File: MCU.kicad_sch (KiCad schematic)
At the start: 16 parts, among them U4 EFM32GG332, Y1 Crystal_GND23

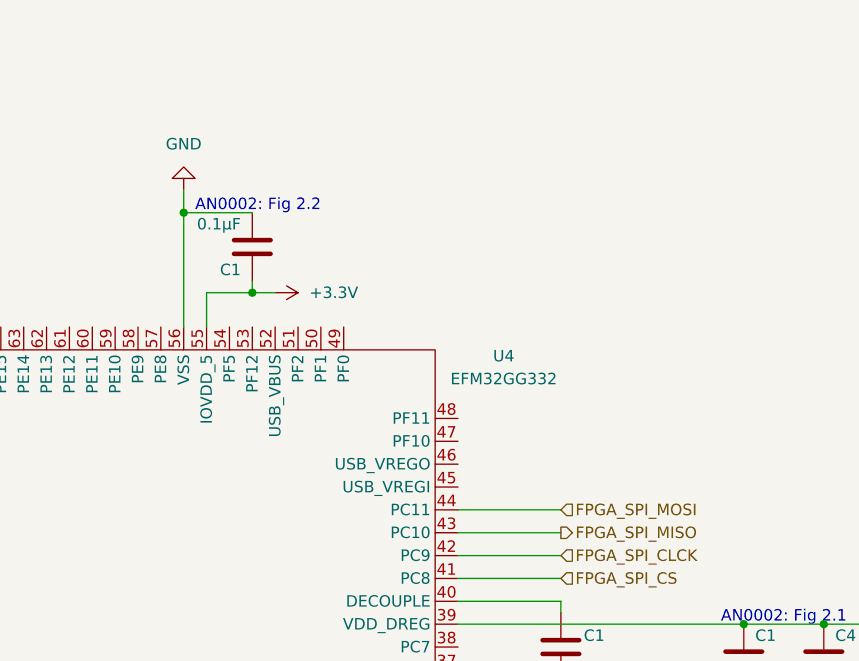
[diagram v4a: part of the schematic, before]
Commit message: Added labels in root for USB signals
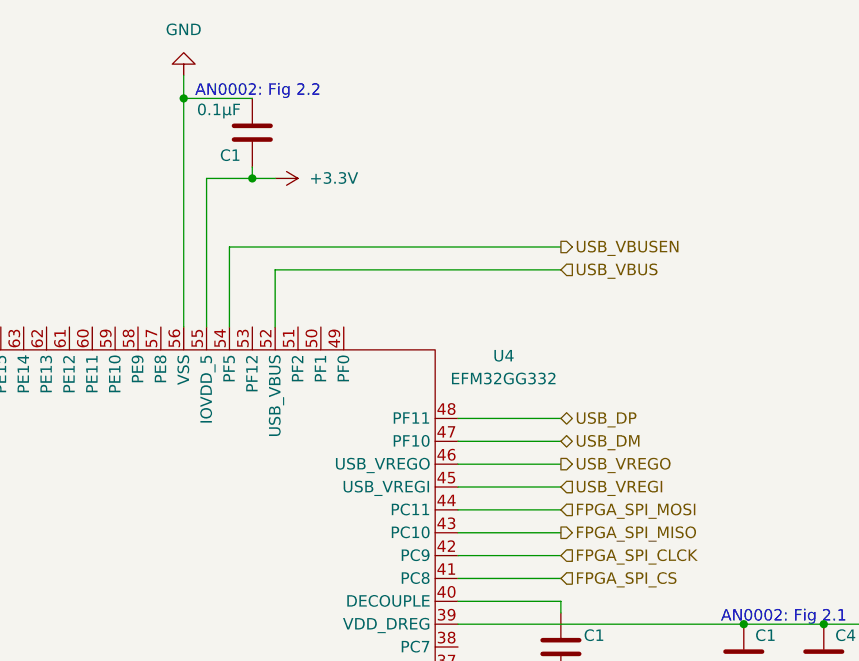
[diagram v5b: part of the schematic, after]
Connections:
- net USB_VREGI: now reaches U4.45 (USB_VREGI)
- net USB_VREGO: now reaches U4.46 (USB_VREGO)
- net USB_DM: now reaches U4.47 (PF10)
- net USB_DP: now reaches U4.48 (PF11)
- net USB_VBUS: now reaches U4.52 (USB_VBUS)
- net USB_VBUSEN: now reaches U4.54 (PF5)
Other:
- moved on the sheet: C1
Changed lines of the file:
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@@
   (junction (at 104.14 133.35) (diameter 0) (color 0 0 0 0)
   )
-  (junction (at 139.7 45.72) (diameter 0) (color 0 0 0 0)
+  (junction (at 139.7 33.02) (diameter 0) (color 0 0 0 0)
   )
   (junction (at 185.42 147.32) (diameter 0) (color 0 0 0 0)
@@
   (junction (at 170.18 147.32) (diameter 0) (color 0 0 0 0)
   )
-  (junction (at 147.32 54.61) (diameter 0) (color 0 0 0 0)
+  (junction (at 147.32 41.91) (diameter 0) (color 0 0 0 0)
   )
   (junction (at 134.62 133.35) (diameter 0) (color 0 0 0 0)
@@
   (junction (at 123.19 133.35) (diameter 0) (color 0 0 0 0)
   )
+  (wire (pts (xy 170.18 73.66) (xy 181.61 73.66))
+    (stroke (width 0) (type default))
+  )
   (wire (pts (xy 185.42 147.32) (xy 182.88 147.32))
     (stroke (width 0) (type default))
@@
     (stroke (width 0) (type default))
   )
+  (wire (pts (xy 144.78 58.42) (xy 144.78 49.53))
+    (stroke (width 0) (type default))
+  )
   (wire (pts (xy 101.6 81.28) (xy 106.68 81.28))
     (stroke (width 0) (type default))
@@
     (stroke (width 0) (type default))
   )
+  (wire (pts (xy 149.86 58.42) (xy 149.86 52.07))
+    (stroke (width 0) (type default))
+  )
   (wire (pts (xy 185.42 157.48) (xy 185.42 156.21))
     (stroke (width 0) (type default))
@@
     (stroke (width 0) (type default))
   )
-  (wire (pts (xy 139.7 45.72) (xy 147.32 45.72))
+  (wire (pts (xy 139.7 33.02) (xy 147.32 33.02))
+    (stroke (width 0) (type default))
+  )
+  (wire (pts (xy 149.86 52.07) (xy 181.61 52.07))
     (stroke (width 0) (type default))
   )
@@
     (stroke (width 0) (type default))
   )
+  (wire (pts (xy 170.18 71.12) (xy 181.61 71.12))
+    (stroke (width 0) (type default))
+  )
   (wire (pts (xy 93.98 133.35) (xy 104.14 133.35))
     (stroke (width 0) (type default))
@@
     (stroke (width 0) (type default))
   )
+  (wire (pts (xy 170.18 68.58) (xy 181.61 68.58))
+    (stroke (width 0) (type default))
+  )
   (wire (pts (xy 125.73 140.97) (xy 132.08 140.97))
     (stroke (width 0) (type default))
@@
     (stroke (width 0) (type default))
   )
-  (wire (pts (xy 147.32 54.61) (xy 147.32 53.34))
+  (wire (pts (xy 147.32 41.91) (xy 147.32 40.64))
+    (stroke (width 0) (type default))
+  )
+  (wire (pts (xy 170.18 76.2) (xy 181.61 76.2))
+    (stroke (width 0) (type default))
+  )
+  (wire (pts (xy 144.78 49.53) (xy 181.61 49.53))
     (stroke (width 0) (type default))
   )
@@
     (stroke (width 0) (type default))
   )
+  (wire (pts (xy 142.24 41.91) (xy 142.24 58.42))
+    (stroke (width 0) (type default))
+  )
   (wire (pts (xy 170.18 139.7) (xy 137.16 139.7))
     (stroke (width 0) (type default))
   )
-  (wire (pts (xy 147.32 54.61) (xy 149.86 54.61))
+  (wire (pts (xy 147.32 41.91) (xy 149.86 41.91))
     (stroke (width 0) (type default))
   )
@@
     (stroke (width 0) (type default))
   )
-  (wire (pts (xy 139.7 43.18) (xy 139.7 45.72))
+  (wire (pts (xy 139.7 30.48) (xy 139.7 33.02))
     (stroke (width 0) (type default))
   )
@@
     (stroke (width 0) (type default))
   )
-  (wire (pts (xy 139.7 45.72) (xy 139.7 58.42))
+  (wire (pts (xy 139.7 33.02) (xy 139.7 58.42))
     (stroke (width 0) (type default))
   )
@@
     (stroke (width 0) (type default))
   )
-  (wire (pts (xy 142.24 58.42) (xy 142.24 54.61))
-    (stroke (width 0) (type default))
-  )
   (wire (pts (xy 125.73 133.35) (xy 134.62 133.35))
     (stroke (width 0) (type default))
@@
     (stroke (width 0) (type default))
   )
-  (wire (pts (xy 142.24 54.61) (xy 147.32 54.61))
+  (wire (pts (xy 142.24 41.91) (xy 147.32 41.91))
     (stroke (width 0) (type default))
   )
@@
     (effects (font (size 1.27 1.27)) (justify left bottom))
   )
-  (text "AN0002: Fig 2.2" (at 140.97 45.72 0)
+  (text "AN0002: Fig 2.2" (at 140.97 33.02 0)
     (effects (font (size 1.27 1.27)) (justify left bottom))
   )
@@
     (effects (font (size 1.27 1.27)) (justify right bottom))
   )
+  (hierarchical_label "USB_DM" (shape bidirectional) (at 181.61 71.12 0) (fields_autoplaced)
+    (effects (font (size 1.27 1.27)) (justify left))
+  )
   (hierarchical_label "FPGA_SPI_CS" (shape input) (at 181.61 86.36 0) (fields_autoplaced)
     (effects (font (size 1.27 1.27)) (justify left))
   )
+  (hierarchical_label "USB_VBUSEN" (shape output) (at 181.61 49.53 0) (fields_autoplaced)
+    (effects (font (size 1.27 1.27)) (justify left))
+  )
   (hierarchical_label "FPGA_SPI_CLCK" (shape input) (at 181.61 83.82 0) (fields_autoplaced)
+    (effects (font (size 1.27 1.27)) (justify left))
+  )
+  (hierarchical_label "USB_VREGI" (shape input) (at 181.61 76.2 0) (fields_autoplaced)
     (effects (font (size 1.27 1.27)) (justify left))
   )
@@
     (effects (font (size 1.27 1.27)) (justify right))
   )
+  (hierarchical_label "USB_VBUS" (shape input) (at 181.61 52.07 0) (fields_autoplaced)
+    (effects (font (size 1.27 1.27)) (justify left))
+  )
   (hierarchical_label "FPGA_RESET" (shape output) (at 161.29 121.92 0) (fields_autoplaced)
     (effects (font (size 1.27 1.27)) (justify left))
@@
     (effects (font (size 1.27 1.27)) (justify right))
   )
+  (hierarchical_label "USB_VREGO" (shape output) (at 181.61 73.66 0) (fields_autoplaced)
+    (effects (font (size 1.27 1.27)) (justify left))
+  )
   (hierarchical_label "FPGA_SPI_MOSI" (shape input) (at 181.61 78.74 0) (fields_autoplaced)
     (effects (font (size 1.27 1.27)) (justify left))
@@
   (hierarchical_label "Button 6" (shape input) (at 101.6 81.28 180) (fields_autoplaced)
     (effects (font (size 1.27 1.27)) (justify right))
+  )
+  (hierarchical_label "USB_DP" (shape bidirectional) (at 181.61 68.58 0) (fields_autoplaced)
+    (effects (font (size 1.27 1.27)) (justify left))
   )
   (hierarchical_label "Button 4" (shape input) (at 101.6 76.2 180) (fields_autoplaced)
@@
     )
   )
-  (symbol (lib_id "power:+3.3V") (at 149.86 54.61 270) (unit 1)
+  (symbol (lib_id "power:+3.3V") (at 149.86 41.91 270) (unit 1)
     (in_bom yes) (on_board yes) (dnp no) (fields_autoplaced)
-    (property "Reference" "#PWR040" (at 146.05 54.61 0)
-      (effects (font (size 1.27 1.27)) hide)
-    )
-    (property "Value" "+3.3V" (at 153.67 54.61 90)
-      (effects (font (size 1.27 1.27)) (justify left))
-    )
-    (property "Footprint" "" (at 149.86 54.61 0)
-      (effects (font (size 1.27 1.27)) hide)
-    )
-    (property "Datasheet" "" (at 149.86 54.61 0)
+    (property "Reference" "#PWR040" (at 146.05 41.91 0)
+      (effects (font (size 1.27 1.27)) hide)
+    )
+    (property "Value" "+3.3V" (at 153.67 41.91 90)
+      (effects (font (size 1.27 1.27)) (justify left))
+    )
+    (property "Footprint" "" (at 149.86 41.91 0)
+      (effects (font (size 1.27 1.27)) hide)
+    )
+    (property "Datasheet" "" (at 149.86 41.91 0)
       (effects (font (size 1.27 1.27)) hide)
     )
@@
     )
   )
-  (symbol (lib_id "Device:C") (at 147.32 49.53 180) (unit 1)
+  (symbol (lib_id "Device:C") (at 147.32 36.83 180) (unit 1)
     (in_bom yes) (on_board yes) (dnp no)
-    (property "Reference" "C1" (at 146.05 52.07 0)
-      (effects (font (size 1.27 1.27)) (justify left))
-    )
-    (property "Value" "0.1µF" (at 146.05 46.99 0)
-      (effects (font (size 1.27 1.27)) (justify left))
-    )
-    (property "Footprint" "" (at 146.3548 45.72 0)
-      (effects (font (size 1.27 1.27)) hide)
-    )
-    (property "Datasheet" "~" (at 147.32 49.53 0)
+    (property "Reference" "C1" (at 146.05 39.37 0)
+      (effects (font (size 1.27 1.27)) (justify left))
+    )
+    (property "Value" "0.1µF" (at 146.05 34.29 0)
+      (effects (font (size 1.27 1.27)) (justify left))
+    )
+    (property "Footprint" "" (at 146.3548 33.02 0)
+      (effects (font (size 1.27 1.27)) hide)
+    )
+    (property "Datasheet" "~" (at 147.32 36.83 0)
       (effects (font (size 1.27 1.27)) hide)
     )
@@
     )
   )
-  (symbol (lib_id "power:GND") (at 139.7 43.18 180) (unit 1)
+  (symbol (lib_id "power:GND") (at 139.7 30.48 180) (unit 1)
     (in_bom yes) (on_board yes) (dnp no) (fields_autoplaced)
-    (property "Reference" "#PWR01" (at 139.7 36.83 0)
-      (effects (font (size 1.27 1.27)) hide)
-    )
-    (property "Value" "GND" (at 139.7 38.1 0)
-      (effects (font (size 1.27 1.27)))
-    )
-    (property "Footprint" "" (at 139.7 43.18 0)
-      (effects (font (size 1.27 1.27)) hide)
-    )
-    (property "Datasheet" "" (at 139.7 43.18 0)
-      (effects (font (size 1.27 1.27)) hide)
-    )
+    (property "Reference" "#PWR01" (at 139.7 24.13 0)
+      (effects (font (size 1.27 1.27)) hide)
+    )
+    (property "Value" "GND" (at 139.7 25.4 0)
+      (effects (font (size 1.27 1.27)))
+    )
+    (property "Footprint" "" (at 139.7 30.48 0)
+      (effects (font (size 1.27 1.27)) hide)
+    )
+    (property "Datasheet" "" (at 139.7 30.48 0)
+      (effects (font (size 1.27 1.27)) hide)
+    )

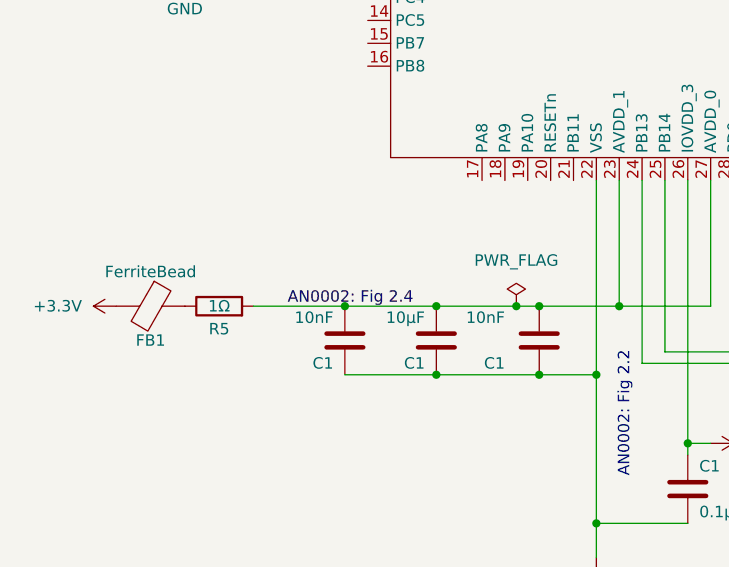
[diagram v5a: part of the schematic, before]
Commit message: Changed AVCC from ferrite bead to 3.3VA
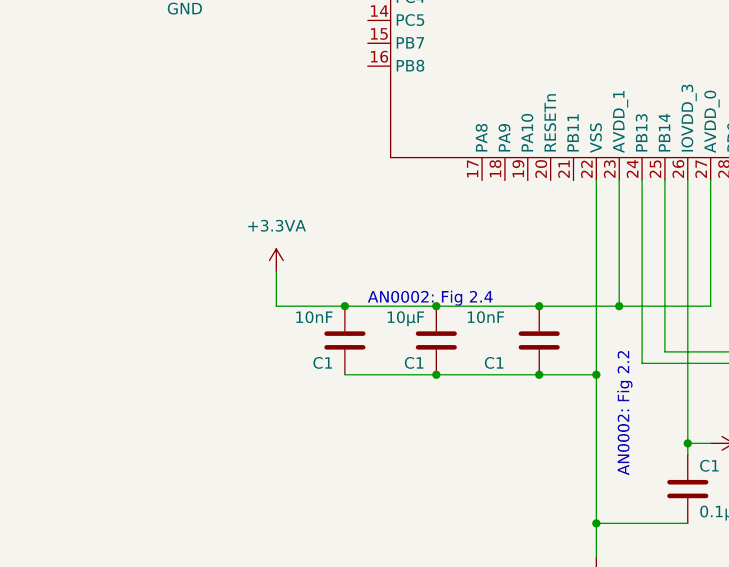
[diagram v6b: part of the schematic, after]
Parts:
- removed FB1: FerriteBead, symbol Device:FerriteBead
- removed R5: 1Ω, symbol Device:R
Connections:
- net AN0002: Fig 2.4 renamed +3.3VA
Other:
- note added: "AN0002: Fig 2.4"
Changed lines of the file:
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@@
   (junction (at 142.24 148.59) (diameter 0) (color 0 0 0 0)
   )
+  (junction (at 139.7 33.02) (diameter 0) (color 0 0 0 0)
+  )
+  (junction (at 185.42 147.32) (diameter 0) (color 0 0 0 0)
+  )
+  (junction (at 132.08 140.97) (diameter 0) (color 0 0 0 0)
+  )
+  (junction (at 125.73 140.97) (diameter 0) (color 0 0 0 0)
+  )
+  (junction (at 114.3 133.35) (diameter 0) (color 0 0 0 0)
+  )
+  (junction (at 170.18 147.32) (diameter 0) (color 0 0 0 0)
+  )
+  (junction (at 147.32 41.91) (diameter 0) (color 0 0 0 0)
+  )
+  (junction (at 134.62 133.35) (diameter 0) (color 0 0 0 0)
+  )
+  (junction (at 210.82 91.44) (diameter 0) (color 0 0 0 0)
+  )
+  (junction (at 114.3 140.97) (diameter 0) (color 0 0 0 0)
+  )
   (junction (at 104.14 133.35) (diameter 0) (color 0 0 0 0)
   )
-  (junction (at 139.7 33.02) (diameter 0) (color 0 0 0 0)
-  )
-  (junction (at 185.42 147.32) (diameter 0) (color 0 0 0 0)
-  )
-  (junction (at 132.08 140.97) (diameter 0) (color 0 0 0 0)
-  )
-  (junction (at 125.73 140.97) (diameter 0) (color 0 0 0 0)
-  )
-  (junction (at 114.3 133.35) (diameter 0) (color 0 0 0 0)
-  )
-  (junction (at 170.18 147.32) (diameter 0) (color 0 0 0 0)
-  )
-  (junction (at 147.32 41.91) (diameter 0) (color 0 0 0 0)
-  )
-  (junction (at 134.62 133.35) (diameter 0) (color 0 0 0 0)
-  )
-  (junction (at 210.82 91.44) (diameter 0) (color 0 0 0 0)
-  )
-  (junction (at 114.3 140.97) (diameter 0) (color 0 0 0 0)
-  )
   (junction (at 179.07 157.48) (diameter 0) (color 0 0 0 0)
   )
-  (junction (at 123.19 133.35) (diameter 0) (color 0 0 0 0)
-  )
   (wire (pts (xy 170.18 73.66) (xy 181.61 73.66))
     (stroke (width 0) (type default))
@@
     (stroke (width 0) (type default))
   )
+  (wire (pts (xy 96.52 133.35) (xy 104.14 133.35))
+    (stroke (width 0) (type default))
+  )
   (wire (pts (xy 175.26 147.32) (xy 170.18 147.32))
     (stroke (width 0) (type default))
@@
     (stroke (width 0) (type default))
   )
-  (wire (pts (xy 93.98 133.35) (xy 104.14 133.35))
+  (wire (pts (xy 114.3 133.35) (xy 125.73 133.35))
     (stroke (width 0) (type default))
   )
@@
     (stroke (width 0) (type default))
   )
-  (wire (pts (xy 123.19 133.35) (xy 125.73 133.35))
-    (stroke (width 0) (type default))
-  )
   (wire (pts (xy 170.18 157.48) (xy 179.07 157.48))
     (stroke (width 0) (type default))
@@
     (stroke (width 0) (type default))
   )
-  (wire (pts (xy 114.3 133.35) (xy 123.19 133.35))
-    (stroke (width 0) (type default))
-  )
   (wire (pts (xy 142.24 148.59) (xy 142.24 149.86))
     (stroke (width 0) (type default))
   )
   (wire (pts (xy 179.07 157.48) (xy 179.07 158.75))
+    (stroke (width 0) (type default))
+  )
+  (wire (pts (xy 96.52 129.54) (xy 96.52 133.35))
     (stroke (width 0) (type default))
   )
@@
     (effects (font (size 1.27 1.27)) (justify left bottom))
   )
+  (text "AN0002: Fig 2.4" (at 106.68 133.35 0)
+    (effects (font (size 1.27 1.27)) (justify left bottom))
+  )
   (text "AN0002: Fig 2.2" (at 140.97 33.02 0)
     (effects (font (size 1.27 1.27)) (justify left bottom))
   )
-  (label "AN0002: Fig 2.4" (at 111.76 133.35 180) (fields_autoplaced)
-    (effects (font (size 1.27 1.27)) (justify right bottom))
-  )
   (hierarchical_label "USB_DM" (shape bidirectional) (at 181.61 71.12 0) (fields_autoplaced)
     (effects (font (size 1.27 1.27)) (justify left))
@@
         (path "/fba50eda-8593-4456-af98-ff56fd418a76/ae46c600-e32c-45ef-b9ae-c42d4bac8718"
           (reference "#PWR038") (unit 1)
-        )
-      )
-    )
-  )
-  (symbol (lib_id "power:+3.3V") (at 78.74 133.35 90) (unit 1)
-    (in_bom yes) (on_board yes) (dnp no) (fields_autoplaced)
-    (property "Reference" "#PWR041" (at 82.55 133.35 0)
-      (effects (font (size 1.27 1.27)) hide)
-    )
-    (property "Value" "+3.3V" (at 74.93 133.35 90)
-      (effects (font (size 1.27 1.27)) (justify left))
-    )
-    (property "Footprint" "" (at 78.74 133.35 0)
-      (effects (font (size 1.27 1.27)) hide)
-    )
-    (property "Datasheet" "" (at 78.74 133.35 0)
-      (effects (font (size 1.27 1.27)) hide)
-    )
-    (pin "1")
-    (instances
-      (project "GuitarZero"
-        (path "/fba50eda-8593-4456-af98-ff56fd418a76/ae46c600-e32c-45ef-b9ae-c42d4bac8718"
-          (reference "#PWR041") (unit 1)
         )
       )
@@
     )
   )
-  (symbol (lib_id "Device:R") (at 90.17 133.35 90) (unit 1)
-    (in_bom yes) (on_board yes) (dnp no)
-    (property "Reference" "R5" (at 90.17 135.89 90)
-      (effects (font (size 1.27 1.27)))
-    )
-    (property "Value" "1Ω" (at 90.17 133.35 90)
-      (effects (font (size 1.27 1.27)))
-    )
-    (property "Footprint" "" (at 90.17 135.128 90)
-      (effects (font (size 1.27 1.27)) hide)
-    )
-    (property "Datasheet" "~" (at 90.17 133.35 0)
-      (effects (font (size 1.27 1.27)) hide)
-    )
-    (pin "1")
-    (pin "2")
-    (instances
-      (project "GuitarZero"
-        (path "/fba50eda-8593-4456-af98-ff56fd418a76/2f5e5303-1176-466f-800a-96bac7c62873"
-          (reference "R5") (unit 1)
-        )
-        (path "/fba50eda-8593-4456-af98-ff56fd418a76/ae46c600-e32c-45ef-b9ae-c42d4bac8718"
-          (reference "R18") (unit 1)
-        )
-      )
-    )
-  )
   (symbol (lib_id "Device:C") (at 142.24 153.67 0) (unit 1)
     (in_bom yes) (on_board yes) (dnp no)
@@
         (path "/fba50eda-8593-4456-af98-ff56fd418a76/ae46c600-e32c-45ef-b9ae-c42d4bac8718"
           (reference "C62") (unit 1)
-        )
-      )
-    )
-  )
-  (symbol (lib_id "Device:FerriteBead") (at 82.55 133.35 270) (unit 1)
-    (in_bom yes) (on_board yes) (dnp no)
-    (property "Reference" "FB1" (at 82.55 137.16 90)
-      (effects (font (size 1.27 1.27)))
-    )
-    (property "Value" "FerriteBead" (at 82.55 129.54 90)
-      (effects (font (size 1.27 1.27)))
-    )
-    (property "Footprint" "" (at 82.55 131.572 90)
-      (effects (font (size 1.27 1.27)) hide)
-    )
-    (property "Datasheet" "~https://www.we-online.com/components/products/datasheet/74279266.pdf" (at 82.55 133.35 0)
-      (effects (font (size 1.27 1.27)) hide)
-    )
-    (pin "1")
-    (pin "2")
-    (instances
-      (project "GuitarZero"
-        (path "/fba50eda-8593-4456-af98-ff56fd418a76/2f5e5303-1176-466f-800a-96bac7c62873"
-          (reference "FB1") (unit 1)
-        )
-        (path "/fba50eda-8593-4456-af98-ff56fd418a76/ae46c600-e32c-45ef-b9ae-c42d4bac8718"
-          (reference "FB2") (unit 1)
         )
       )
@@
     )
   )
+  (symbol (lib_id "power:+3.3VA") (at 96.52 129.54 0) (unit 1)
+    (in_bom yes) (on_board yes) (dnp no) (fields_autoplaced)
+    (property "Reference" "#PWR041" (at 96.52 133.35 0)
+      (effects (font (size 1.27 1.27)) hide)
+    )
+    (property "Value" "+3.3VA" (at 96.52 124.46 0)
+      (effects (font (size 1.27 1.27)))
+    )
+    (property "Footprint" "" (at 96.52 129.54 0)
+      (effects (font (size 1.27 1.27)) hide)
+    )
+    (property "Datasheet" "" (at 96.52 129.54 0)
+      (effects (font (size 1.27 1.27)) hide)
+    )
+    (pin "1")
+    (instances
+      (project "GuitarZero"
+        (path "/fba50eda-8593-4456-af98-ff56fd418a76/ae46c600-e32c-45ef-b9ae-c42d4bac8718"
+          (reference "#PWR041") (unit 1)
+        )
+      )
+    )
+  )
   (symbol (lib_id "power:GND") (at 172.72 140.97 0) (unit 1)
     (in_bom yes) (on_board yes) (dnp no)
@@
         )
       )
-    )
-  )
-  (symbol (lib_id "power:PWR_FLAG") (at 123.19 133.35 0) (unit 1)
-    (in_bom yes) (on_board yes) (dnp no) (fields_autoplaced)
-    (property "Reference" "#FLG05" (at 123.19 131.445 0)
-      (effects (font (size 1.27 1.27)) hide)
-    )
-    (property "Value" "PWR_FLAG" (at 123.19 128.27 0)
-      (effects (font (size 1.27 1.27)))
-    )
-    (property "Footprint" "" (at 123.19 133.35 0)
-      (effects (font (size 1.27 1.27)) hide)
-    )
-    (property "Datasheet" "~" (at 123.19 133.35 0)
-      (effects (font (size 1.27 1.27)) hide)
-    )
-    (pin "1")
-    (instances
-      (project "GuitarZero"
-        (path "/fba50eda-8593-4456-af98-ff56fd418a76/ae46c600-e32c-45ef-b9ae-c42d4bac8718"
-          (reference "#FLG05") (unit 1)
-        )
-      )
